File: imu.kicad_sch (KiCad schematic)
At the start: 21 parts, among them U3 IIS2MDCTR, U4 LSM6DSO32TR, U5 TMP108AIYFFR, U6 BME280

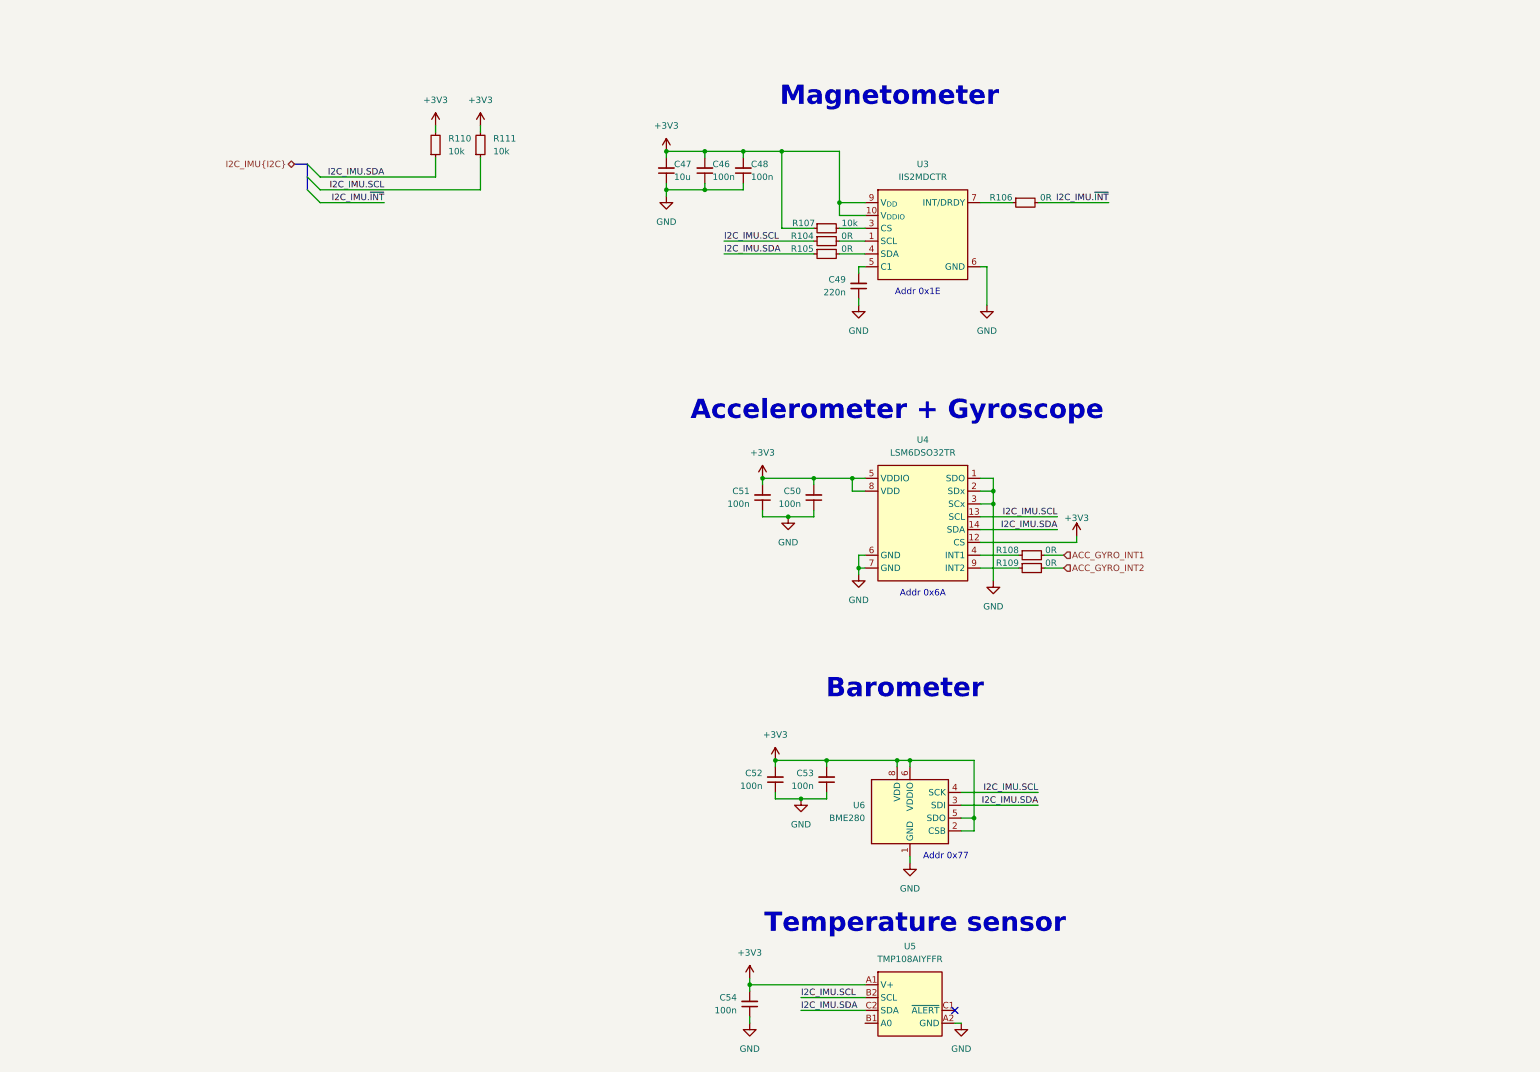
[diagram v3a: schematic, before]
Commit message: [#95036] Reconnect IMU interupts
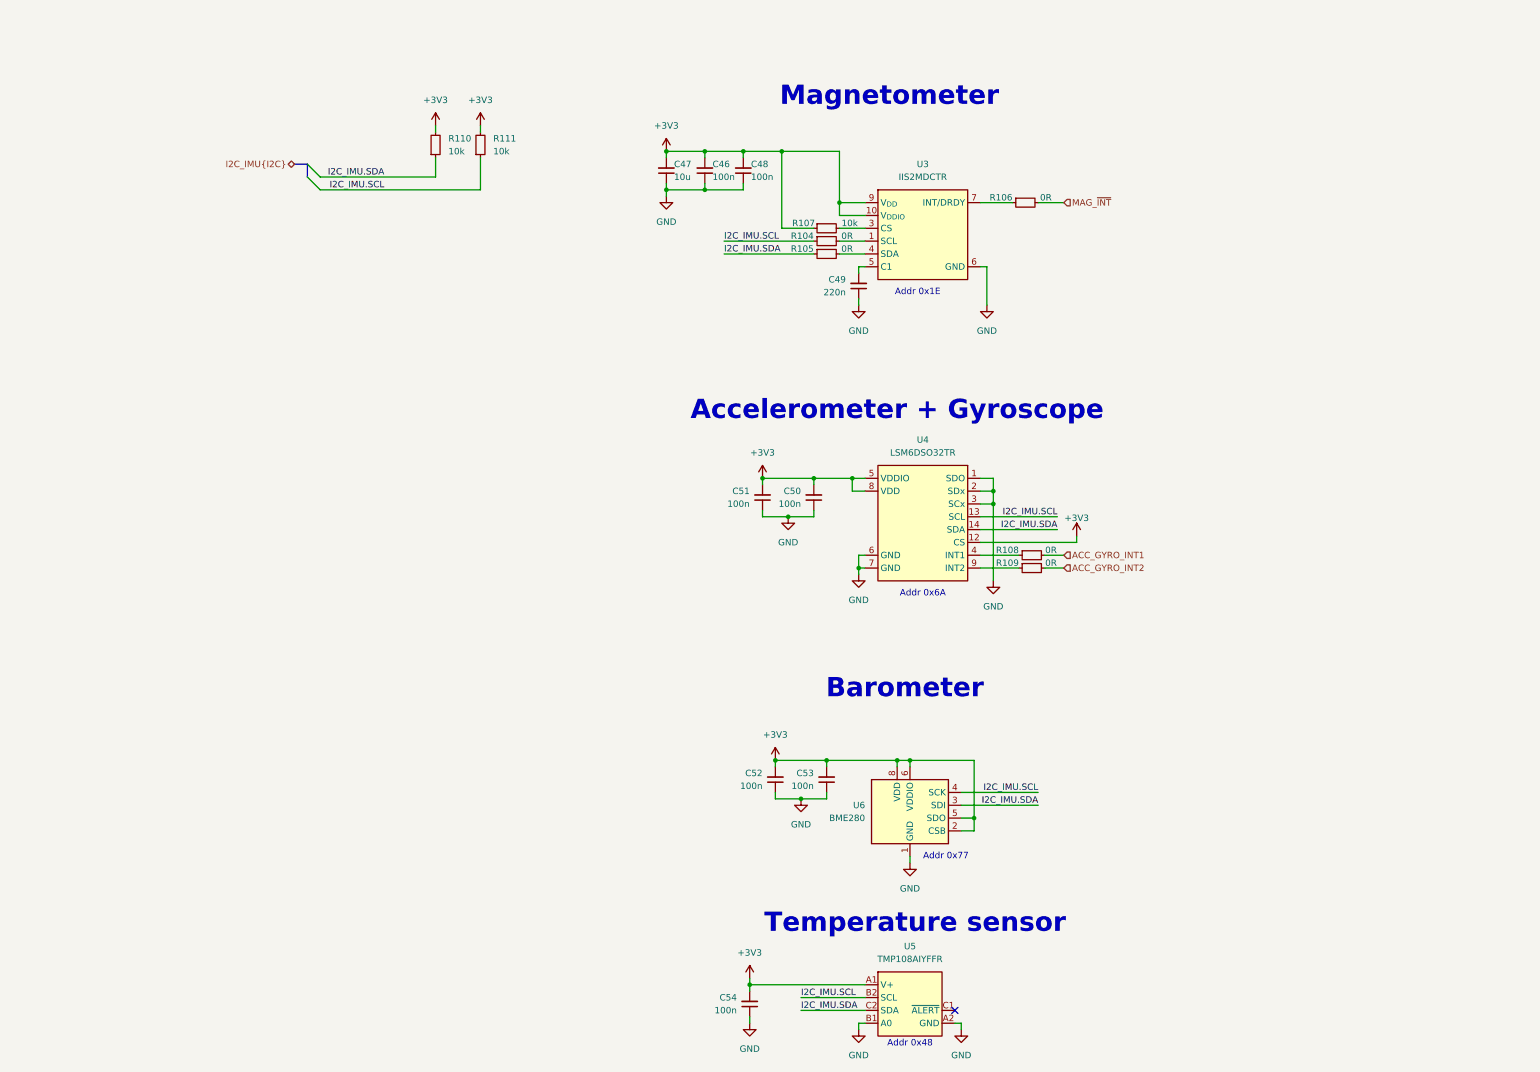
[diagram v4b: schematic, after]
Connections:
- net GND: now also U5.B1 (A0)
- net I2C_IMU.~{INT} renamed MAG_~{INT}
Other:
- note added: "Addr 0x48"
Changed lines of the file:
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@@
 		)
 	)
+	(text "Addr 0x48\n\n"
+		(exclude_from_sim no)
+		(at 219.71 254 0)
+		(effects
+			(font
+				(size 1.27 1.27)
+			)
+		)
+	)
 	(junction
 		(at 171.45 76.2)
@@
 		)
 	)
-	(bus_entry
-		(at 100.33 83.82)
-		(size 2.54 2.54)
-		(stroke
-			(width 0)
-			(type default)
-		)
-	)
 	(wire
 		(pts
@@
 	(wire
 		(pts
-			(xy 245.11 86.36) (xy 259.08 86.36)
+			(xy 245.11 86.36) (xy 250.19 86.36)
 		)
 		(stroke
@@
 	(wire
 		(pts
+			(xy 209.55 248.92) (xy 209.55 250.19)
+		)
+		(stroke
+			(width 0)
+			(type default)
+		)
+	)
+	(wire
+		(pts
 			(xy 210.82 156.21) (xy 209.55 156.21)
 		)
@@
 	(wire
 		(pts
-			(xy 203.2 196.85) (xy 203.2 198.12)
+			(xy 229.87 248.92) (xy 229.87 250.19)
 		)
 		(stroke
@@
 	(wire
 		(pts
-			(xy 134.62 83.82) (xy 134.62 77.47)
+			(xy 203.2 196.85) (xy 203.2 198.12)
 		)
 		(stroke
@@
 		)
 	)
-	(bus
+	(wire
 		(pts
-			(xy 100.33 81.28) (xy 100.33 83.82)
+			(xy 134.62 83.82) (xy 134.62 77.47)
 		)
 		(stroke
@@
 	(wire
 		(pts
-			(xy 102.87 86.36) (xy 115.57 86.36)
-		)
-		(stroke
-			(width 0)
-			(type default)
-		)
-	)
-	(wire
-		(pts
 			(xy 229.87 210.82) (xy 232.41 210.82)
 		)
@@
 	(wire
 		(pts
+			(xy 210.82 248.92) (xy 209.55 248.92)
+		)
+		(stroke
+			(width 0)
+			(type default)
+		)
+	)
+	(wire
+		(pts
 			(xy 219.71 215.9) (xy 219.71 217.17)
 		)
@@
 		)
 	)
-	(label "I2C_IMU.~{INT}"
-		(at 115.57 86.36 180)
-		(effects
-			(font
-				(size 1.27 1.27)
-			)
-			(justify right bottom)
-		)
-	)
 	(label "I2C_IMU.SDA"
 		(at 115.57 81.28 180)
@@
 		)
 	)
-	(label "I2C_IMU.~{INT}"
-		(at 259.08 86.36 180)
-		(effects
-			(font
-				(size 1.27 1.27)
-			)
-			(justify right bottom)
-		)
-	)
 	(hierarchical_label "ACC_GYRO_INT1"
 		(shape input)
@@
 		)
 	)
+	(hierarchical_label "MAG_~{INT}"
+		(shape input)
+		(at 250.19 86.36 0)
+		(effects
+			(font
+				(size 1.27 1.27)
+			)
+			(justify left)
+		)
+	)
 	(symbol
 		(lib_id "antmicropower:GND")
@@
 	(symbol
 		(lib_id "antmicropower:GND")
-		(at 229.87 248.92 0)
+		(at 229.87 250.19 0)
 		(mirror y)
 		(unit 1)
@@
 		(fields_autoplaced yes)
 		(property "Reference" "#PWR0125"
-			(at 220.98 251.46 0)
+			(at 220.98 252.73 0)
 			(effects
 				(font
@@
 		)
 		(property "Value" "GND"
-			(at 229.87 254 0)
+			(at 229.87 255.27 0)
 			(effects
 				(font
@@
 		)
 		(property "Footprint" ""
-			(at 220.98 256.54 0)
+			(at 220.98 257.81 0)
 			(effects
 				(font
@@
 		)
 		(property "Datasheet" ""
-			(at 220.98 261.62 0)
+			(at 220.98 262.89 0)
 			(effects
 				(font
@@
 		)
 		(property "Description" ""
-			(at 220.98 264.16 0)
+			(at 220.98 265.43 0)
 			(effects
 				(font
@@
 		)
 		(property "Author" "Antmicro"
-			(at 220.98 256.54 0)
+			(at 220.98 257.81 0)
 			(effects
 				(font
@@
 		)
 		(property "License" "Apache-2.0"
-			(at 220.98 259.08 0)
+			(at 220.98 260.35 0)
 			(effects
 				(font
@@
 					(unit 1)
 				)
+			)
+		)
+	)
+	(symbol
+		(lib_id "antmicropower:GND")
+		(at 209.55 250.19 0)
+		(mirror y)
+		(unit 1)
+		(exclude_from_sim no)
+		(in_bom yes)
+		(on_board yes)
+		(dnp no)
+		(fields_autoplaced yes)
+		(property "Reference" "#PWR0166"
+			(at 200.66 252.73 0)
+			(effects
+				(font
+					(size 1.27 1.27)
+					(thickness 0.15)
+				)
+				(justify left bottom)
+				(hide yes)
+			)
+		)
+		(property "Value" "GND"
+			(at 209.55 255.27 0)
+			(effects
+				(font
+					(size 1.27 1.27)
+					(thickness 0.15)
+				)
+			)
+		)
+		(property "Footprint" ""
+			(at 200.66 257.81 0)
+			(effects
+				(font
+					(size 1.27 1.27)
+					(thickness 0.15)
+				)
+				(justify left bottom)
+				(hide yes)
+			)
+		)
+		(property "Datasheet" ""
+			(at 200.66 262.89 0)
+			(effects
+				(font
+					(size 1.27 1.27)
+					(thickness 0.15)
+				)
+				(justify left bottom)
+				(hide yes)
+			)
+		)
+		(property "Description" ""
+			(at 200.66 265.43 0)
+			(effects
+				(font
+					(size 1.27 1.27)
+				)
+				(justify left bottom)
+				(hide yes)
+			)
+		)
+		(property "Author" "Antmicro"
+			(at 200.66 257.81 0)
+			(effects
+				(font
+					(size 1.27 1.27)
+					(thickness 0.15)
+				)
+				(justify left bottom)
+				(hide yes)
+			)
+		)
+		(property "License" "Apache-2.0"
+			(at 200.66 260.35 0)
+			(effects
+				(font
+					(size 1.27 1.27)
+					(thickness 0.15)
+				)
+				(justify left bottom)
+				(hide yes)
+			)
+		)
+		(pin "1"
+		)
+		(instances
+			(project "renode-reference-platform"
+				(path "/126ae87b-f292-4372-94ff-ae46971d67ab/143ac980-6d59-4a8b-9ea3-64cd140d4a49"
+					(reference "#PWR0166")
+					(unit 1)
+				)

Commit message: [#95036] Replace barometer IC
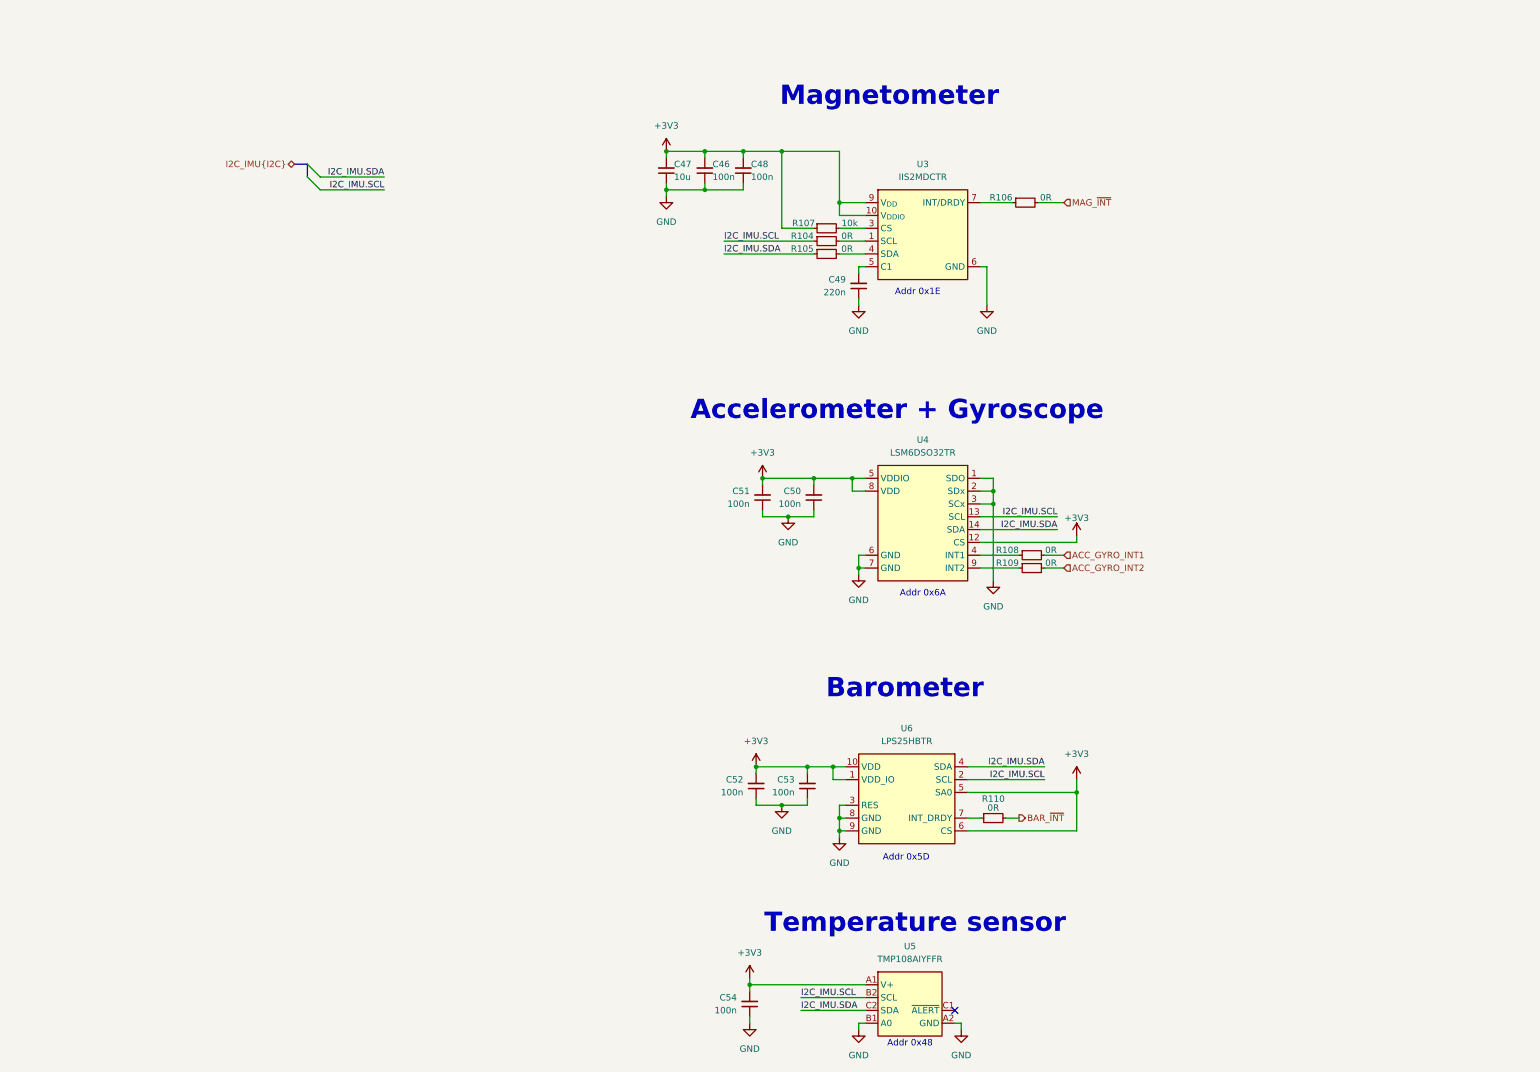
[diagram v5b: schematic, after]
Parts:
- removed R110, R111: R_10k_0402, antmicro-footprints:R_0402_1005Metric, symbol antmicroResistors0402:R_10k_0402
- removed U6: BME280, antmicro-footprints:LGA-8_2.5x2.5mm_BME280, symbol antmicroHumidityMoistureSensors:BME280
- added R110: R_0R_0402, antmicro-footprints:R_0402_1005Metric, symbol antmicroResistors0402:R_0R_0402
- added U6: LPS25HBTR, antmicro-footprints:HLGA-10L_2.5x2.5mm_P0.6mm, symbol antmicroMotionSensorsIMUsInertialMeasurementUnits:LPS25HBTR
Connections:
- net +3V3: now also U6.1 (VDD_IO), U6.10 (VDD), U6.5 (SA0), U6.6 (CS)
- net GND: now also U6.3 (RES), U6.8 (GND), U6.9 (GND)
- net I2C_IMU.SCL: now also U6.2 (SCL)
- net I2C_IMU.SDA: now also U6.4 (SDA)
- new net: R110.1, U6.7 (INT_DRDY)
- new net BAR_~{INT}: R110.2
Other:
- note added: "Addr 0x5D"
- note removed: "Addr 0x77"
- moved on the sheet: C52, C53

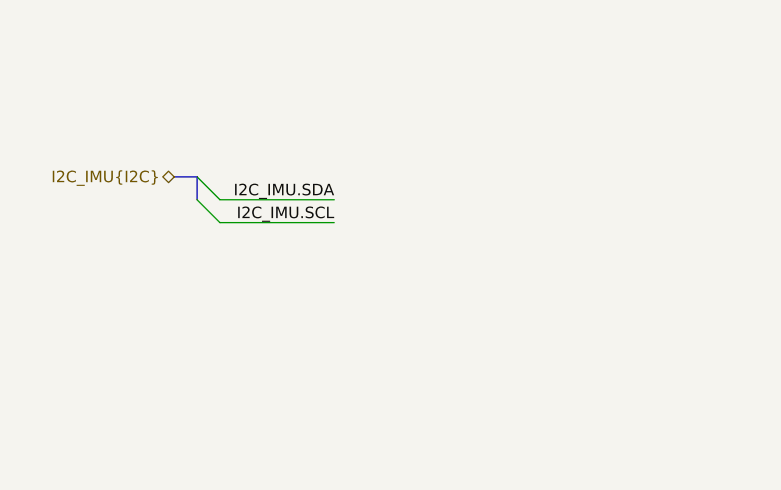
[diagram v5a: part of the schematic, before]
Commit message: [#95036] Add testpoints
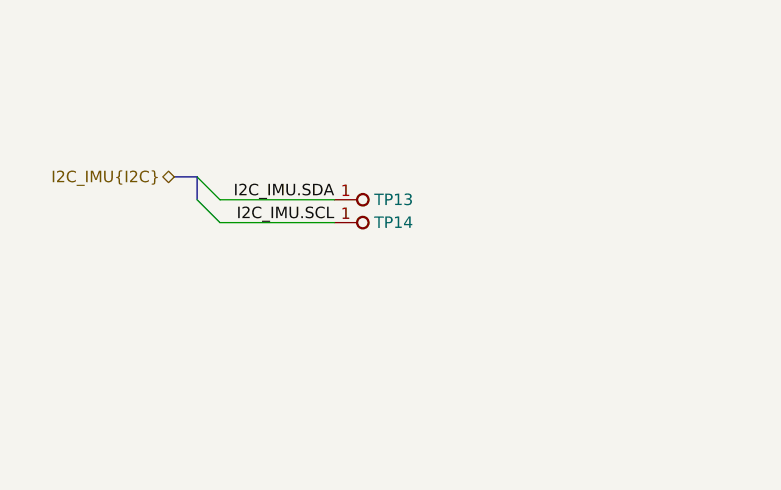
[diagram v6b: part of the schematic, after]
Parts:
- added TP13, TP14: TP_1mm_SMD, antmicro-footprints:TP_SMD_1mm, symbol antmicroTestPoints:TP_1mm_SMD
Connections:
- net I2C_IMU.SCL: now also TP14.1
- net I2C_IMU.SDA: now also TP13.1
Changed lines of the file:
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@@
+	)
+	(symbol
+		(lib_id "antmicroTestPoints:TP_1mm_SMD")
+		(at 115.57 83.82 0)
+		(unit 1)
+		(exclude_from_sim no)
+		(in_bom no)
+		(on_board yes)
+		(dnp no)
+		(property "Reference" "TP14"
+			(at 122.174 83.82 0)
+			(effects
+				(font
+					(size 1.27 1.27)
+					(thickness 0.15)
+				)
+			)
+		)
+		(property "Value" "TP_1mm_SMD"
+			(at 130.81 91.44 0)
+			(effects
+				(font
+					(size 1.27 1.27)
+					(thickness 0.15)
+				)
+				(justify left bottom)
+				(hide yes)
+			)
+		)
+		(property "Footprint" "antmicro-footprints:TP_SMD_1mm"
+			(at 130.81 93.98 0)
+			(effects
+				(font
+					(size 1.27 1.27)
+					(thickness 0.15)
+				)
+				(justify left bottom)
+				(hide yes)
+			)
+		)
+		(property "Datasheet" ""
+			(at 133.35 96.52 0)
+			(effects
+				(font
+					(size 1.27 1.27)
+					(thickness 0.15)
+				)
+				(justify left bottom)
+				(hide yes)
+			)
+		)
+		(property "Description" "Test point 1mm SMD"
+			(at 130.81 104.14 0)
+			(effects
+				(font
+					(size 1.27 1.27)
+				)
+				(justify left bottom)
+				(hide yes)
+			)
+		)
+		(property "MPN" ""
+			(at 115.57 83.82 0)
+			(effects
+				(font
+					(size 1.27 1.27)
+				)
+				(hide yes)
+			)
+		)
+		(property "Manufacturer" ""
+			(at 115.57 83.82 0)
+			(effects
+				(font
+					(size 1.27 1.27)
+				)
+				(hide yes)
+			)
+		)
+		(property "Author" "Antmicro"
+			(at 130.81 99.06 0)
+			(effects
+				(font
+					(size 1.27 1.27)
+					(thickness 0.15)
+				)
+				(justify left bottom)
+				(hide yes)
+			)
+		)
+		(property "License" "Apache-2.0"
+			(at 130.81 101.6 0)
+			(effects
+				(font
+					(size 1.27 1.27)
+					(thickness 0.15)
+				)
+				(justify left bottom)
+				(hide yes)
+			)
+		)
+		(pin "1"
+		)
+		(instances
+			(project "renode-reference-platform"
+				(path "/126ae87b-f292-4372-94ff-ae46971d67ab/143ac980-6d59-4a8b-9ea3-64cd140d4a49"
+					(reference "TP14")
+					(unit 1)
+				)
+			)
+		)
 	)
 	(symbol
@@
 					(unit 1)
 				)
+			)
+		)
+	)
+	(symbol
+		(lib_id "antmicroTestPoints:TP_1mm_SMD")
+		(at 115.57 81.28 0)
+		(unit 1)
+		(exclude_from_sim no)
+		(in_bom no)
+		(on_board yes)
+		(dnp no)
+		(property "Reference" "TP13"
+			(at 122.174 81.28 0)
+			(effects
+				(font
+					(size 1.27 1.27)
+					(thickness 0.15)
+				)
+			)
+		)
+		(property "Value" "TP_1mm_SMD"
+			(at 130.81 88.9 0)
+			(effects
+				(font
+					(size 1.27 1.27)
+					(thickness 0.15)
+				)
+				(justify left bottom)
+				(hide yes)
+			)
+		)
+		(property "Footprint" "antmicro-footprints:TP_SMD_1mm"
+			(at 130.81 91.44 0)
+			(effects
+				(font
+					(size 1.27 1.27)
+					(thickness 0.15)
+				)
+				(justify left bottom)
+				(hide yes)
+			)
+		)
+		(property "Datasheet" ""
+			(at 133.35 93.98 0)
+			(effects
+				(font
+					(size 1.27 1.27)
+					(thickness 0.15)
+				)
+				(justify left bottom)
+				(hide yes)
+			)
+		)
+		(property "Description" "Test point 1mm SMD"
+			(at 130.81 101.6 0)
+			(effects
+				(font
+					(size 1.27 1.27)
+				)
+				(justify left bottom)
+				(hide yes)
+			)
+		)
+		(property "MPN" ""
+			(at 115.57 81.28 0)
+			(effects
+				(font
+					(size 1.27 1.27)
+				)
+				(hide yes)
+			)
+		)
+		(property "Manufacturer" ""
+			(at 115.57 81.28 0)
+			(effects
+				(font
+					(size 1.27 1.27)
+				)
+				(hide yes)
+			)
+		)
+		(property "Author" "Antmicro"
+			(at 130.81 96.52 0)
+			(effects
+				(font
+					(size 1.27 1.27)
+					(thickness 0.15)
+				)
+				(justify left bottom)
+				(hide yes)
+			)
+		)
+		(property "License" "Apache-2.0"
+			(at 130.81 99.06 0)
+			(effects
+				(font
+					(size 1.27 1.27)
+					(thickness 0.15)
+				)
+				(justify left bottom)
+				(hide yes)
+			)
+		)
+		(pin "1"
+		)
+		(instances
+			(project "renode-reference-platform"
+				(path "/126ae87b-f292-4372-94ff-ae46971d67ab/143ac980-6d59-4a8b-9ea3-64cd140d4a49"
+					(reference "TP13")
+					(unit 1)
+				)
